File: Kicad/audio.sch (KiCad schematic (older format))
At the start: 70 parts, among them J201 CD Audio In, J202 AC'97 Audio Header, J203 Line Out, U201 TLV320AIC23BPW, U202 STX-4335-5BGP-S1, Y201 12M

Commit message: Switching some parts over to the CPL.
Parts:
- C202, C203, C204, C206, C208, C209, C213, C214, C216, C217: value 10u 10V -> 10u 16V; Digikey 1276-6455-1-ND -> (none); MPN CL21A106KOQNNNG -> CPL-CAP-X5R-0805-10UF-16V; Manufacturer Samsung -> CPL
- C207, C210, C211, C212, C215: Digikey BC1150CT-ND -> (none); MPN K104K15X7RF5TL2 -> CPL-CAP-X7R-0805-100NF-50V; Manufacturer Vishay -> CPL; Mouser 594-K104K15X7RF5TL2 -> (none)
- C220, C221: Digikey 493-15424-ND -> (none); MPN UKT1C221MED -> CPL-CAP-ALU-RAD-220UF-50V; Manufacturer Nichicon -> CPL; Mouser 647-UKT1C221MED -> (none)
- C224: value 1u 10V -> 1u 16V; Digikey 1276-6471-1-ND -> (none); MPN CL21B105KOFNNNG -> CPL-CAP-X7R-0805-1UF-25V; Manufacturer Samsung -> CPL
- FB201, FB202, FB203, FB204, FB205, FB206, FB208, FB209, FB210: value 3k3 -> 330R@100MHz; Digikey 490-1054-1-ND -> (none); MPN BLM21PG221SN1D -> CPL-IND-FER-330OHM-1.5A; Manufacturer Murata -> CPL; Mouser 81-BLM21P221SG -> (none)
- FB207: value 600R@100MHz -> 330R@100MHz; Digikey 240-2399-1-ND -> (none); MPN HZ0805E601R-10 -> CPL-IND-FER-330OHM-1.5A; Manufacturer Laird -> CPL; Mouser 875-HZ0805E601R-10 -> (none)
- R204, R205: Digikey RMCF0805FT100R-ND -> (none); MPN RMCF0805FT100R -> CPL-RES-0805-100-0.125W; Manufacturer Stackpole -> CPL
- R208, R210, R213, R214, R215: Digikey RMCF0805FT4K75-ND -> (none); MPN RMCF0805FT4K75 -> CPL-RES-0805-4.7K-0.125W; Manufacturer Stackpole -> CPL
- R216: Digikey RMCF0805FT10K0-ND -> (none); MPN RMCF0805FT10K0 -> CPL-RES-0805-10K-0.125W; Manufacturer Stackpole -> CPL
- Y201: footprint Crystal:Crystal_HC49-4H_Vertical -> Crystal:Crystal_SMD_5032-2Pin_5.0x3.2mm_HandSoldering; Digikey 535-9037-ND -> 535-9116-1-ND; MPN ABL-12.000MHZ-B2 -> CPL-OSC-CRY-12MHZ-18PF; Manufacturer Abracon -> CPL; Mouser 815-ABL-12-B2 -> 815-ABM3B-12-B2

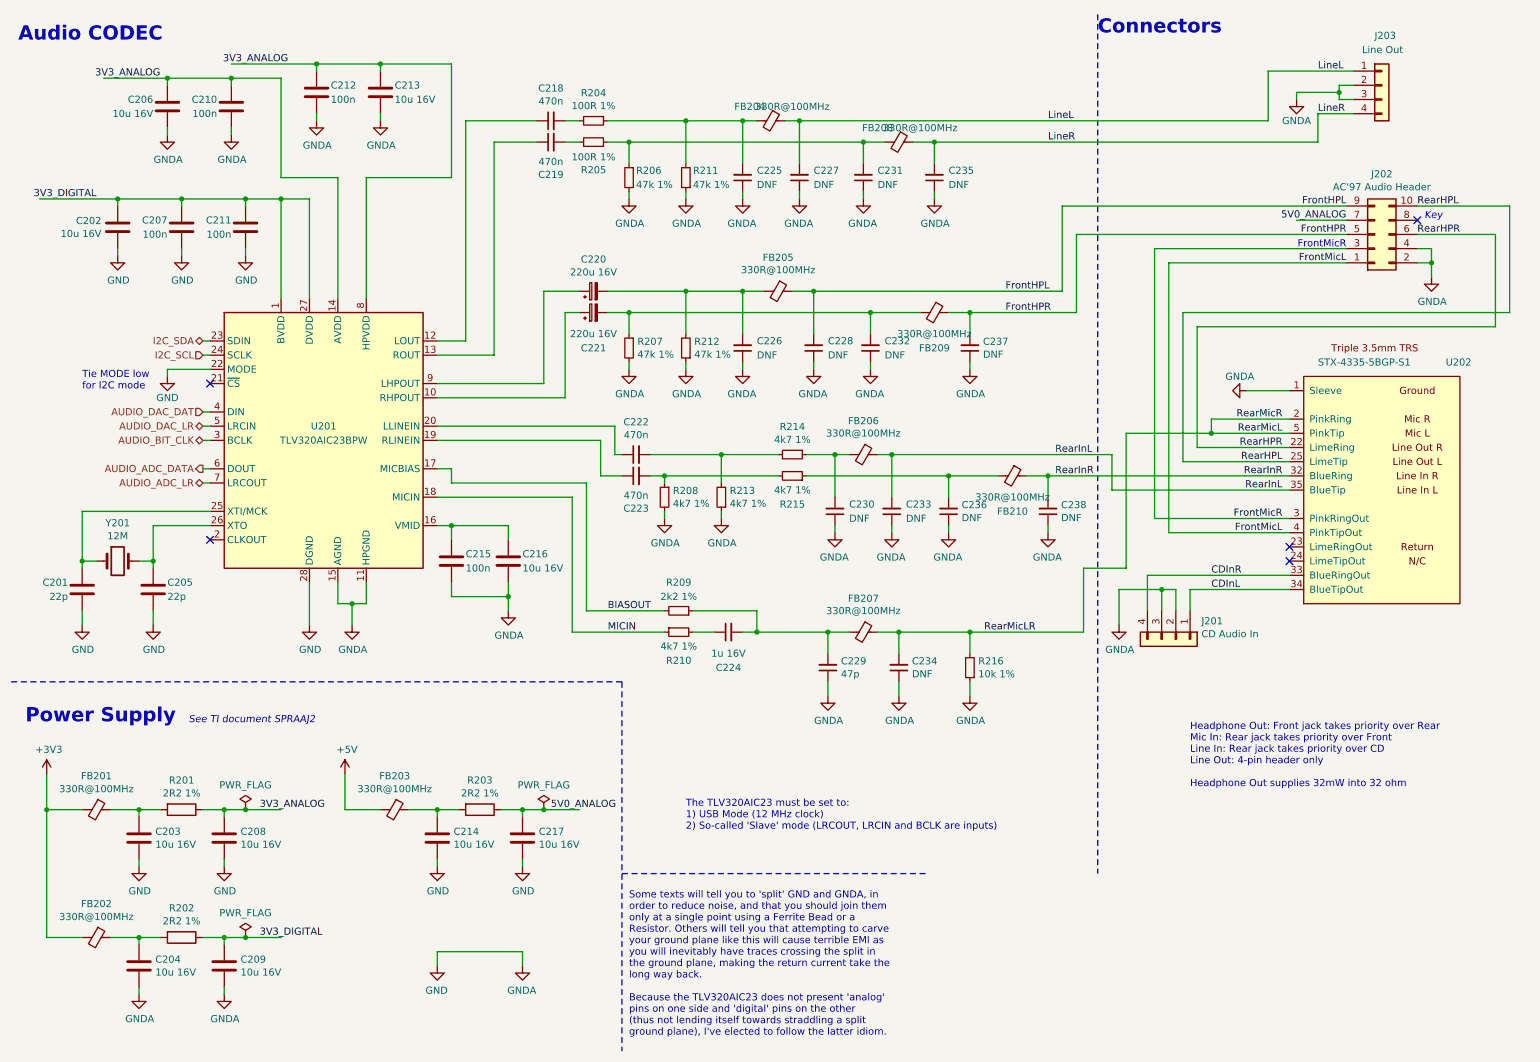
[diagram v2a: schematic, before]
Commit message: Fixing some review comments.
* PCB has rounded corners.
* Add JLCPCB part numbers for SMT parts
* Fixed Fab layer
* Renumbered Slots
* Mounting holes do not have thermal relief

Closes #13 #12 and #10
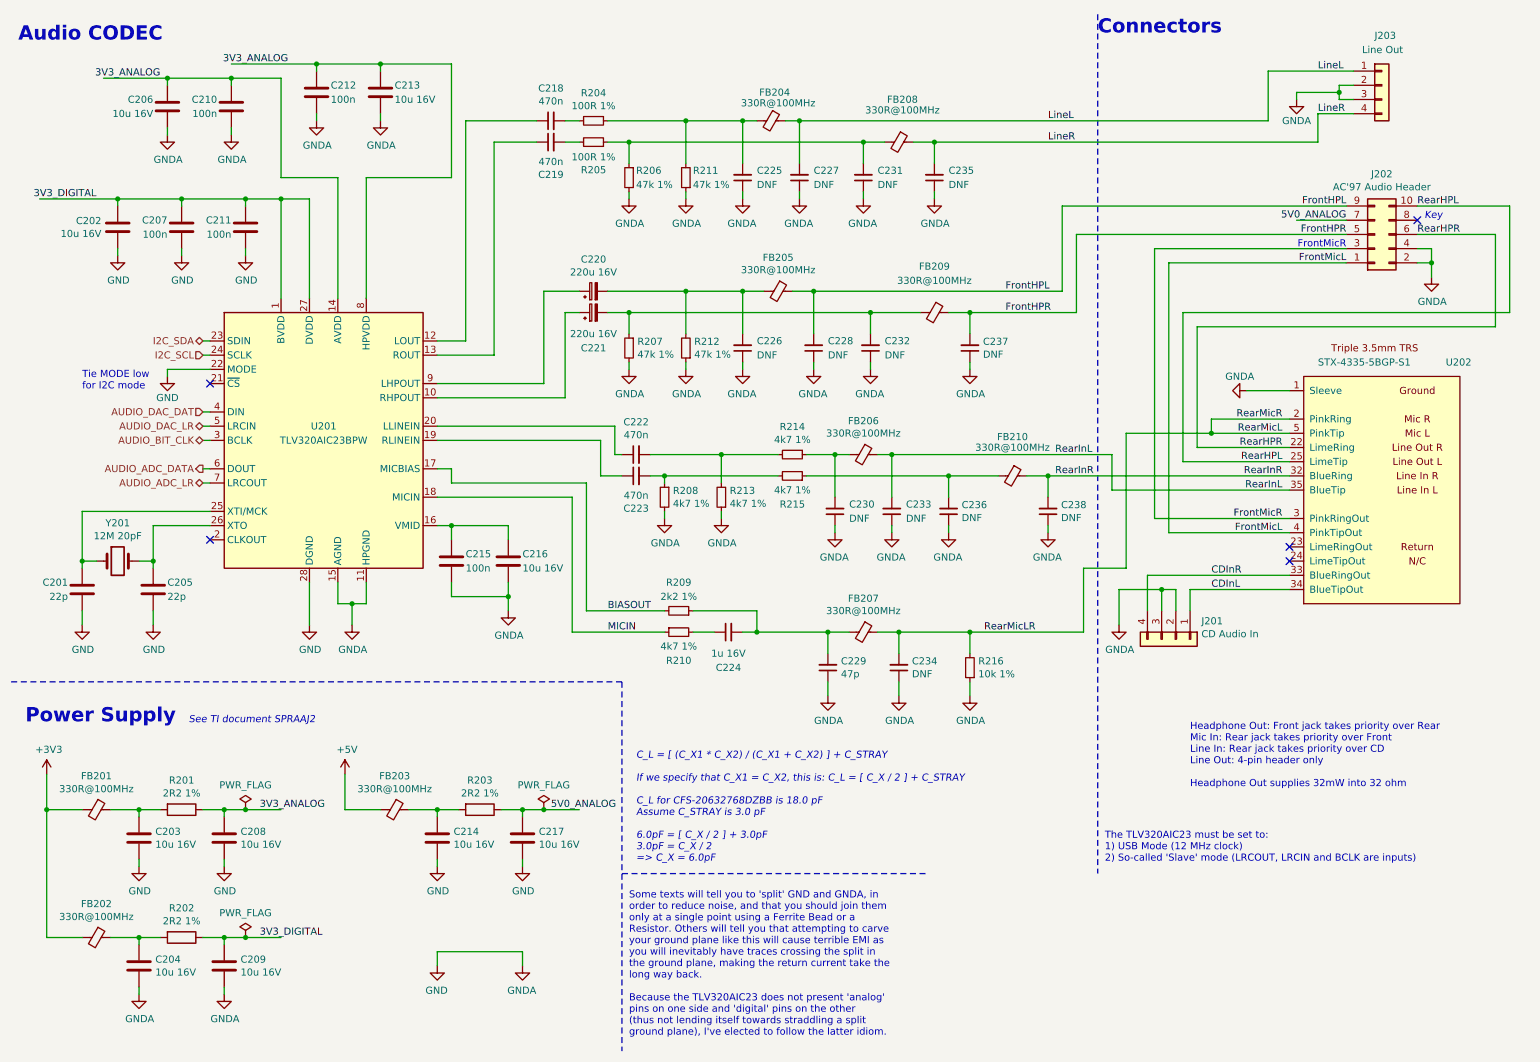
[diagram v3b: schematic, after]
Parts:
- C201, C205: LCSC Part# (none) -> C90883
- C202, C203, C204, C206, C208, C209, C213, C214, C216, C217: LCSC Part# (none) -> C15850
- C207, C210, C211, C212, C215: LCSC Part# (none) -> C49678
- C218, C219, C222, C223: LCSC Part# (none) -> C13967
- C224: LCSC Part# (none) -> C28323
- C229: LCSC Part# (none) -> C14857
- FB201, FB202, FB203, FB204, FB205, FB206, FB207, FB208, FB209, FB210: LCSC Part# (none) -> C1017
- R201, R202, R203: LCSC Part# (none) -> C17521
- R204, R205: LCSC Part# (none) -> C17408
- R206, R207, R211, R212: LCSC Part# (none) -> C17713
- R208, R210, R213, R214, R215: LCSC Part# (none) -> C17673
- R209: LCSC Part# (none) -> C17520
- R216: LCSC Part# (none) -> C17414
- U201: LCSC Part# (none) -> C9915
- Y201: value 12M -> 12M 20pF; Digikey 535-9116-1-ND -> (none); LCSC Part# (none) -> C90883; Mouser 815-ABM3B-12-B2 -> (none)
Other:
- note added: "C_L = [ (C_X1 * C_X2) / (C_X1 + C_X2) ] + C_STRAY\n\nIf we specify that C_X1 = C_X2, this is: C_L = [ C_X / 2 ] + C_STRAY\n\nC_L for CFS-20632768DZBB is 18.0 pF\nAssume C_STRAY is 3.0 pF \n\n6.0pF = [ C_X / 2 ] + 3.0pF\n3.0pF = C_X / 2\n=> C_X = 6.0pF"

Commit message: BoM and PCB fixes.
* Move tolerances and voltages out of value and into their own fields.
* Fix 5V trace for audio stage.
* Fixup docs.yml so outputs work for JLCPCB.
* Fix JLCPCB part number for 22pF caps.
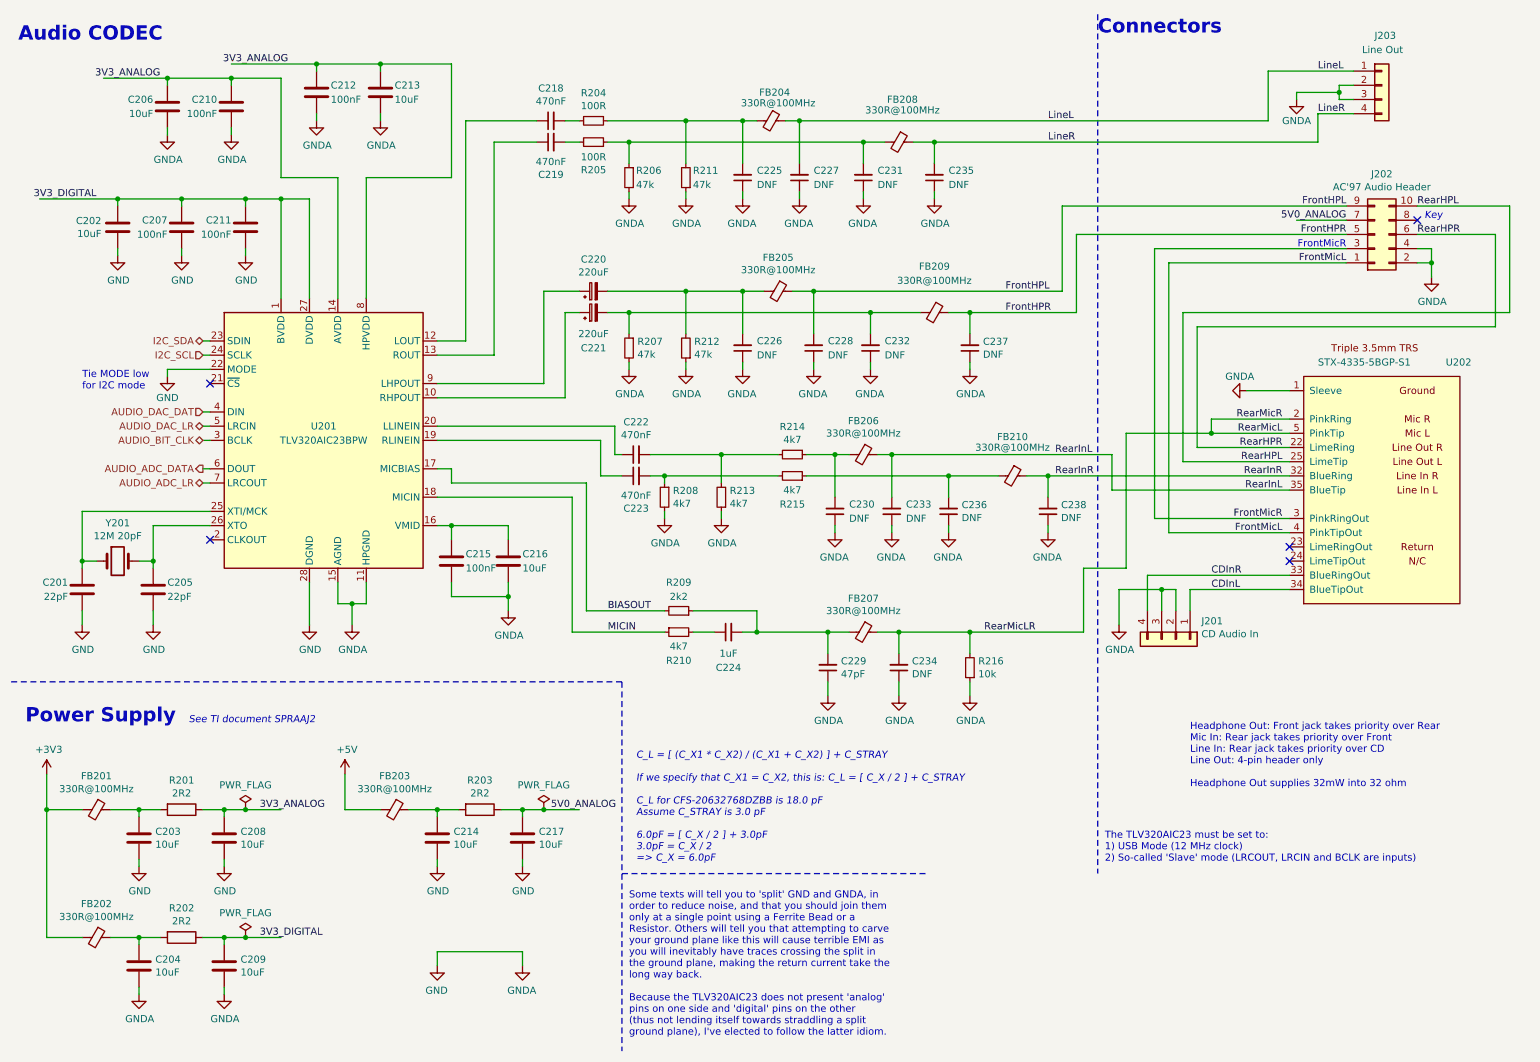
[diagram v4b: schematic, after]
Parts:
- C201, C205: value 22p -> 22pF; LCSC Part# C90883 -> C1804; Voltage (none) -> C0G
- C202, C203, C204, C206, C208, C209, C213, C214, C216, C217: value 10u 16V -> 10uF
- C207, C210, C211, C212, C215: value 100n -> 100nF
- C218, C219, C222, C223: value 470n -> 470nF
- C220, C221: value 220u 16V -> 220uF
- C224: value 1u 16V -> 1uF
- C229: value 47p -> 47pF
- R201, R202, R203: value 2R2 1% -> 2R2
- R204, R205: value 100R 1% -> 100R
- R206, R207, R211, R212: value 47k 1% -> 47k
- R208, R210, R213, R214, R215: value 4k7 1% -> 4k7
- R209: value 2k2 1% -> 2k2
- R216: value 10k 1% -> 10k

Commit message: Feature/swap layers (#22)
* Switch around the layers.

We now have:

1. Signal + Ground
2. Power (3.3V)
3. Ground
4. Signal + Power (3.3V)

This balances things a bit better than Sig/Gnd, Power, Ground, Sig/Gnd.

* Replace MCP7940N with DIP. Also enlarge some caps.

The capacitor footprints were just too small for such large value
electrolytics. The RTC footprint was due to availability.
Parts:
- C220, C221: footprint Capacitor_THT:CP_Radial_D6.3mm_P2.50mm -> Capacitor_THT:CP_Radial_D8.0mm_P5.00mm
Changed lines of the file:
@@
 Sheet 2 11
 Title "Neotron Common Hardware - Audio CODEC"
-Date "2021-06-03"
+Date "2021-06-10"
 Rev "[Uncontrolled]"
 Comp "https://neotron-compute.github.io/"
@@
 F 0 "C220" V 4825 2450 50  0000 C CNN
 F 1 "220uF" V 4734 2450 50  0000 C CNN
-F 2 "Capacitor_THT:CP_Radial_D6.3mm_P2.50mm" H 4600 2450 50  0001 C CNN
+F 2 "Capacitor_THT:CP_Radial_D8.0mm_P5.00mm" H 4600 2450 50  0001 C CNN
 F 3 "~" H 4600 2450 50  0001 C CNN
 F 4 "0" H 4600 2450 50  0001 C CNN "DNP"
@@
 F 0 "C221" V 4350 2600 50  0000 C CNN
 F 1 "220uF" V 4450 2600 50  0000 C CNN
-F 2 "Capacitor_THT:CP_Radial_D6.3mm_P2.50mm" H 4600 2600 50  0001 C CNN
+F 2 "Capacitor_THT:CP_Radial_D8.0mm_P5.00mm" H 4600 2600 50  0001 C CNN
 F 3 "~" H 4600 2600 50  0001 C CNN
 F 4 "0" H 4600 2600 50  0001 C CNN "DNP"
